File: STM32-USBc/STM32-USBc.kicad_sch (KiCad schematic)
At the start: 28 parts, among them J1 Conn_01x04_Pin, J2 Conn_01x04_Pin, J3 Conn_01x04_Pin, P1 USB_C_Plug_USB2.0, SW1 SW_SPDT, U1 STM32F103C8T6, U2 AMS1117-3.3, Y3 16MHz

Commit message: add 3d model for USB c receptacle
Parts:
- C7: value 10n -> 10u
- C8: footprint Capacitor_SMD:C_0603_1608Metric -> Capacitor_SMD:C_0402_1005Metric
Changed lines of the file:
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@@
 			)
 		)
-		(property "Value" "10n"
+		(property "Value" "10u"
 			(at 127 36.8299 0)
 			(effects
@@
 			)
 		)
-		(property "Footprint" "Capacitor_SMD:C_0603_1608Metric"
+		(property "Footprint" "Capacitor_SMD:C_0402_1005Metric"
 			(at 207.9752 38.1 0)
 			(effects

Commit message: 3d model of switch + layout borders
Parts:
- added H1, H2, H3, H4: MountingHole, MountingHole:MountingHole_2.2mm_M2, symbol Mechanical:MountingHole
- SW1: footprint Button_Switch_THT:SW_E-Switch_EG1224_SPDT_Angled -> Button_Switch_SMD:SW_SPDT_CK_JS102011SAQN

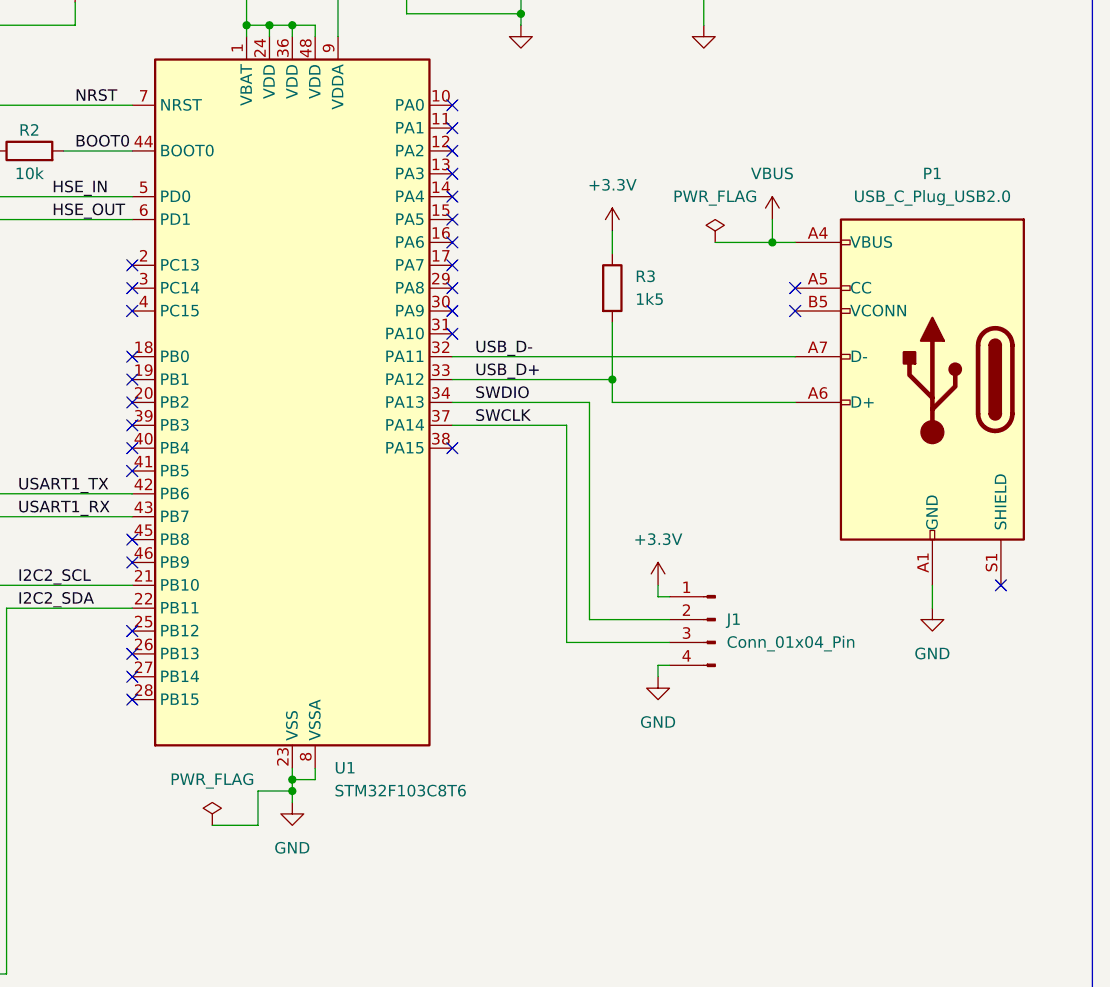
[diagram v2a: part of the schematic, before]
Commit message: switch to usb b
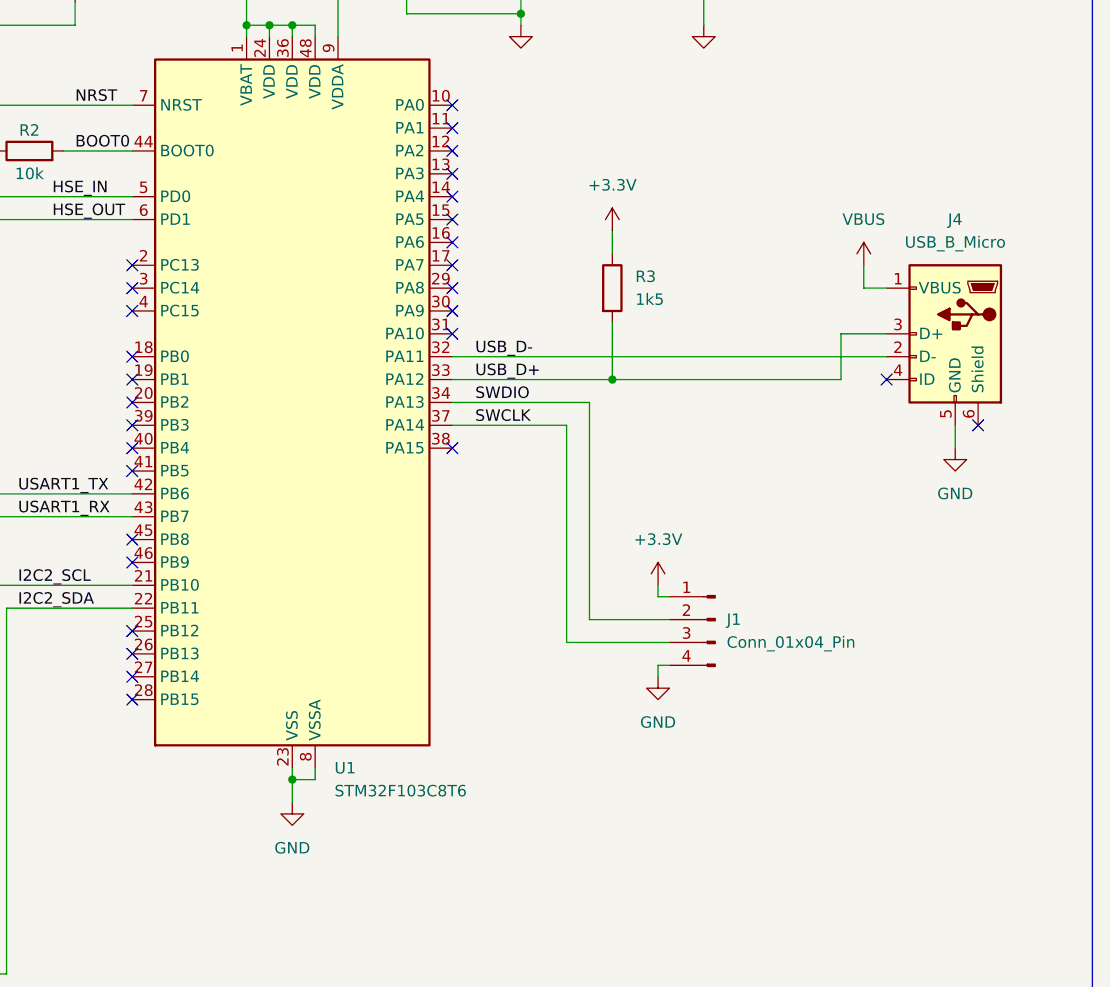
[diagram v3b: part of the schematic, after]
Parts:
- removed P1: USB_C_Plug_USB2.0, Connector_USB:USB_C_Receptacle_Molex_105450-0101, symbol Connector:USB_C_Plug_USB2.0
- added J4: USB_B_Micro, symbol Connector:USB_B_Micro
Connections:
- net GND: now also J4.5 (GND)
- net USB_D+: now also J4.3 (D+)
- net USB_D-: now also J4.2 (D-)
- net VBUS: now also J4.1 (VBUS)
- no-connect marks 30 -> 29
